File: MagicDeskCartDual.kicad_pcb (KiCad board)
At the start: 2 copper layers, 58.4 x 86.2 mm, 11 parts, among them U1 74LS174, U2 74LS02, U3 27C020, U4 C64-Exp-Port, U5 C64-Exp-Port

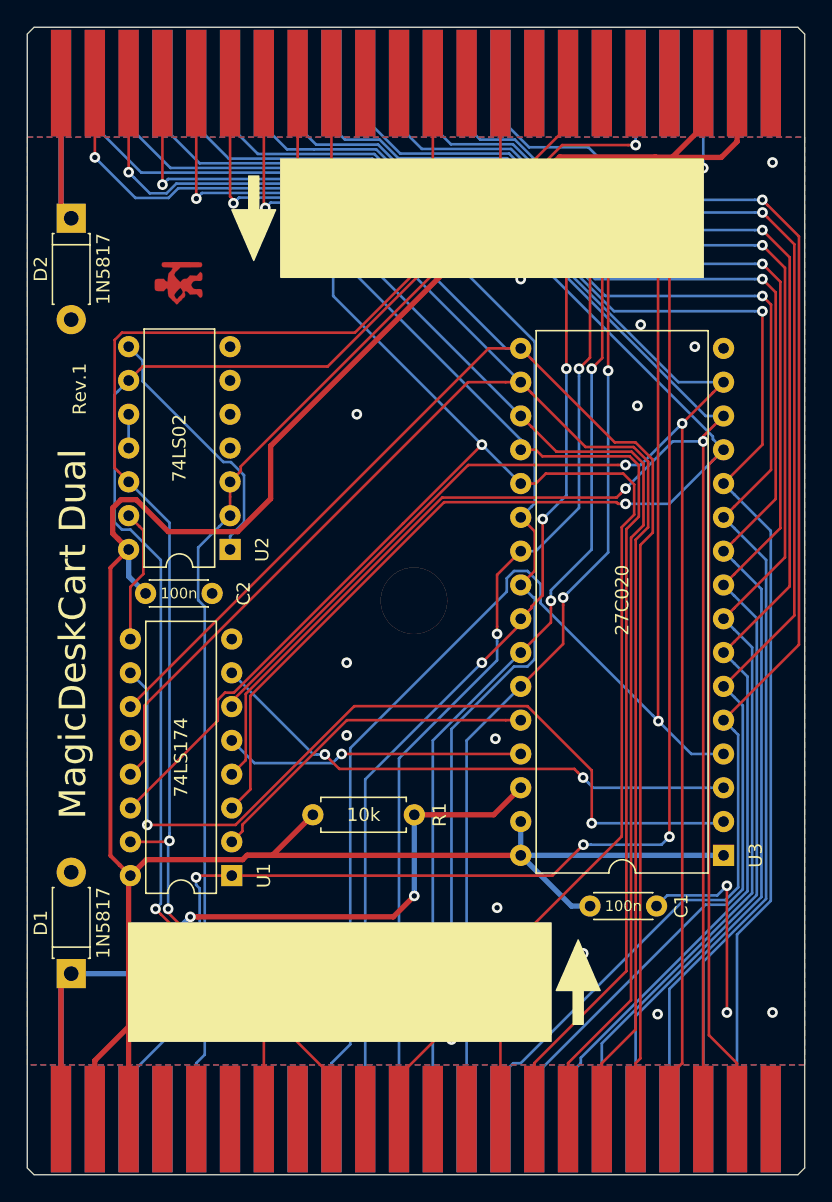
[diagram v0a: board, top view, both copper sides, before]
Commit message: Moved traces away from the board edge.
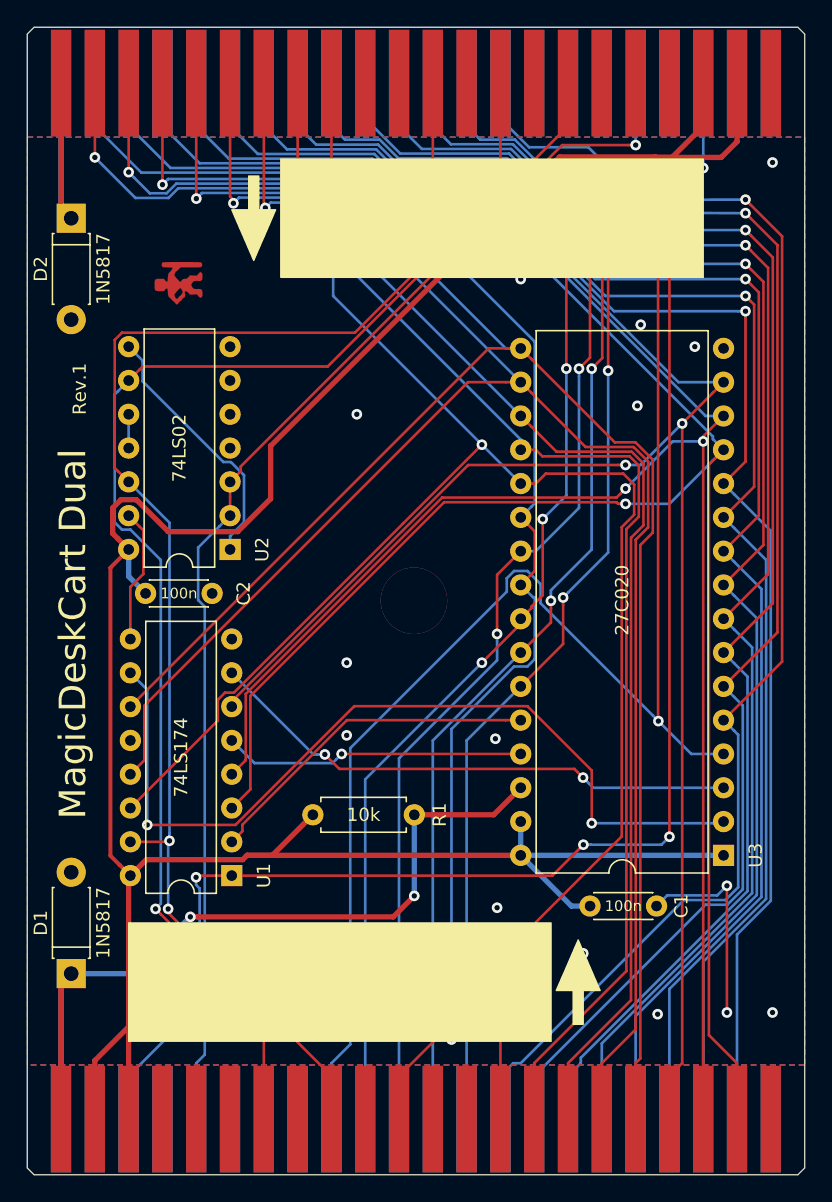
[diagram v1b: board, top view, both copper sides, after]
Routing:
- net /A6: track 120.2 -> 118.4 mm
- net /A5: track 120.0 -> 118.2 mm
- net /A4: track 120.8 -> 119.0 mm
- net /A2: track 122.3 -> 120.5 mm
- net /A3: track 121.5 -> 119.7 mm
- net /A0: track 123.6 -> 121.8 mm
- net /A1: track 123.0 -> 121.2 mm
- net /A7: track 120.5 -> 118.7 mm

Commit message: Added readme.
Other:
- board text added: "Rev.2"
- board text removed: "Rev.1"
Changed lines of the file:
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@@
   )
   (page A4)
+  (title_block
+    (title "MagicDeskCart Dual")
+    (rev 2)
+    (company hackup.net)
+  )
   (layers
     (0 F.Cu signal)
@@
     (effects (font (size 1 1) (thickness 0.15)) (justify mirror))
   )
-  (gr_text Rev.1 (at 81.153 84.709 90) (layer F.SilkS)
+  (gr_text Rev.2 (at 81.153 84.709 90) (layer F.SilkS)
     (effects (font (size 1 1) (thickness 0.15)))
   )
